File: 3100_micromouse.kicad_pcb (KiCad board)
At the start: 2 copper layers, 76 x 76 mm, 31 parts, among them J1 MOTOR1, J10 Extra +3.3V, J11 Extra +5V, J12 Extra +5V, J2 MOTOR2, J3 Extra GPIO A, J4 Extra GPIO B, J5 2 Pin PWR, J6 Aux SPI Bus, J7 Aux I2C Bus, J8 Extra Analog Pins, J9 UART Interface, U1 AMS1117-5.0

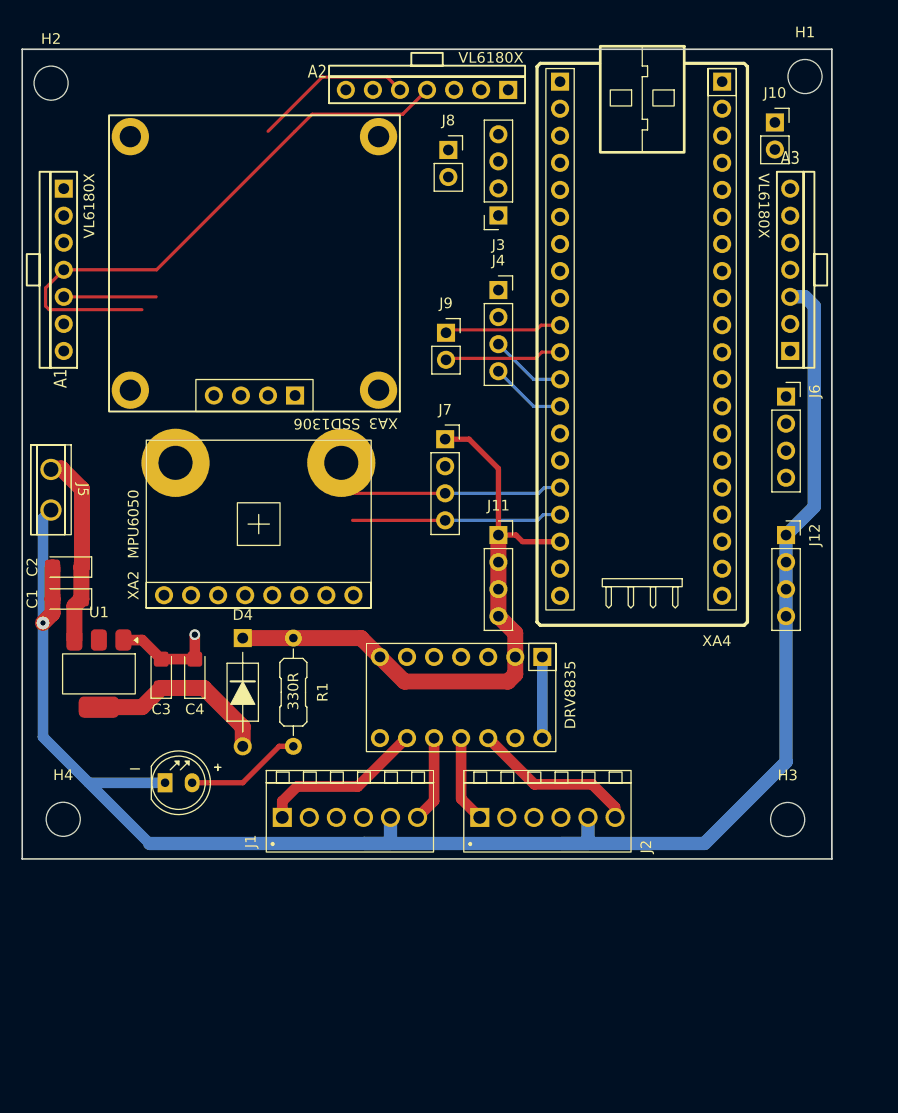
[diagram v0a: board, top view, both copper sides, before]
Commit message: Changed TOF Trigger pins to B12-14 - also removed 3V3 access as board space are running out
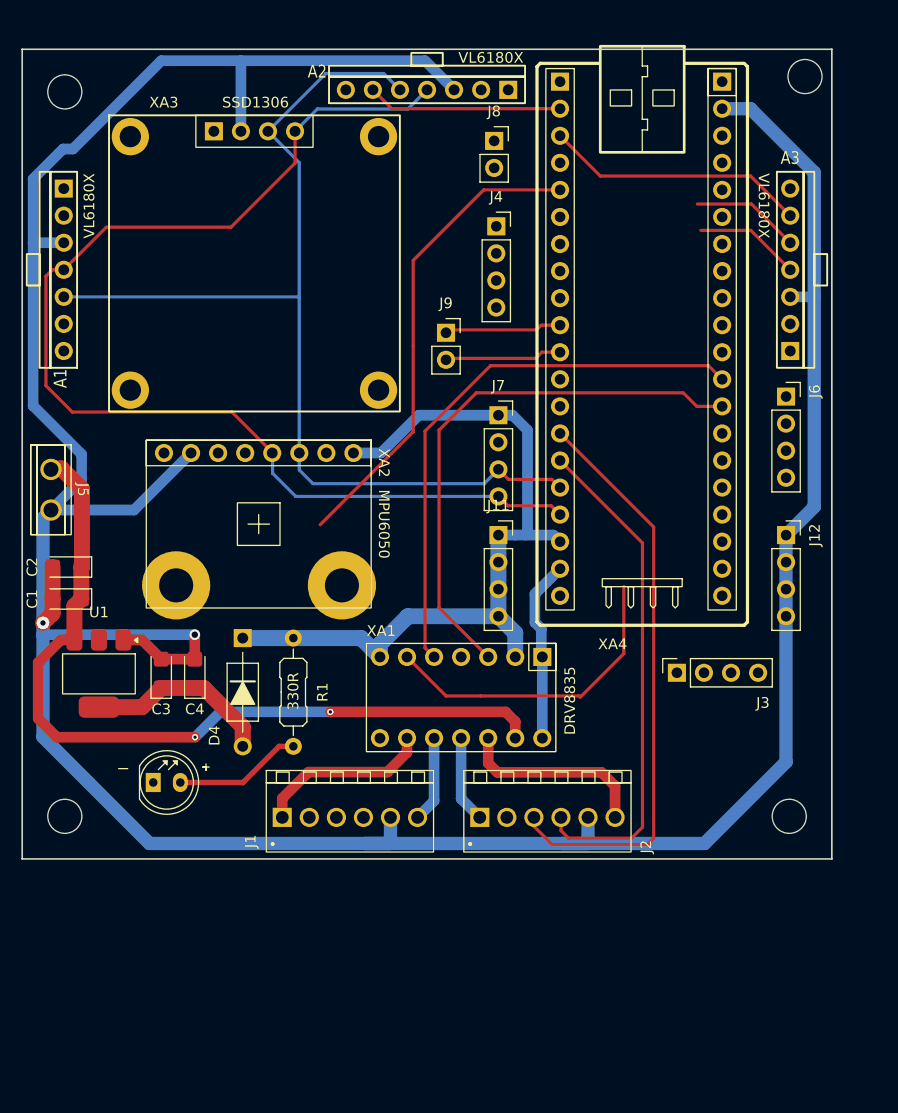
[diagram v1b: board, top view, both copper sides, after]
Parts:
- removed J10: Extra +3.3V, Connector_PinSocket_2.54mm:PinSocket_1x02_P2.54mm_Vertical
- moved J3 46.1 mm to (190.8, 102.9), turned to 90 degrees
- moved J4 5.98 mm to (173.8, 61.0)
- moved J7 5.48 mm to (174.0, 78.8)
- moved J8 4.38 mm to (173.6, 53.0)
- moved H2 1.53 mm to (133.3, 48.4)
- moved D1 1.11 mm to (141.6, 113.2)
- moved H3 0.34 mm to (201.3, 116.4)
- moved H4 0.32 mm to (133.3, 116.4)
- turned XA2 to -90 degrees
- turned XA3 to 0 degrees
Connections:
- J3 pad 1: /B12 -> /C12
- J3 pad 2: /B13 -> /C13
- J3 pad 3: /B14 -> /C14
- XA1 pad 13: VIN -> +9V
- XA4 pad 1: /B12 -> /TRIG1
- XA4 pad 2: /B13 -> /TRIG2
- XA4 pad 22: /TRIG1 -> /C12
- XA4 pad 23: /TRIG2 -> /C13
- XA4 pad 24: /TRIG3 -> /C14
- XA4 pad 3: /B14 -> /TRIG3
- XA4 pad 38: /+3V3 -> /STM32F411 Breakout Pin/+3V3
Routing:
- net GNDREF: track 185.1 -> 329.4 mm
- net /SCL: track 43.4 -> 106.9 mm
- net +9V: track 18.2 -> 76.2 mm, vias 0 -> 2
- net /ENC2A: track 0.00 -> 54.7 mm
- net /PWM1: track 0.00 -> 52.5 mm
- net /PWM2: track 0.00 -> 51.8 mm
- net /ENC2B: track 0.00 -> 47.2 mm
- net /SDA: track 74.1 -> 119.4 mm
- net /ENC1A: track 0.00 -> 44.9 mm
- net /DIR1: track 0.00 -> 29.9 mm
- net /TRIG3: track 0.00 -> 24.7 mm
- net /TRIG2: track 0.00 -> 18.3 mm
- net +5V: track 59.8 -> 74.3 mm
- net /B5: track 7.15 -> 0.00 mm
- net /B4: track 7.15 -> 0.00 mm
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
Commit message: Finialized and Finished PCB routing
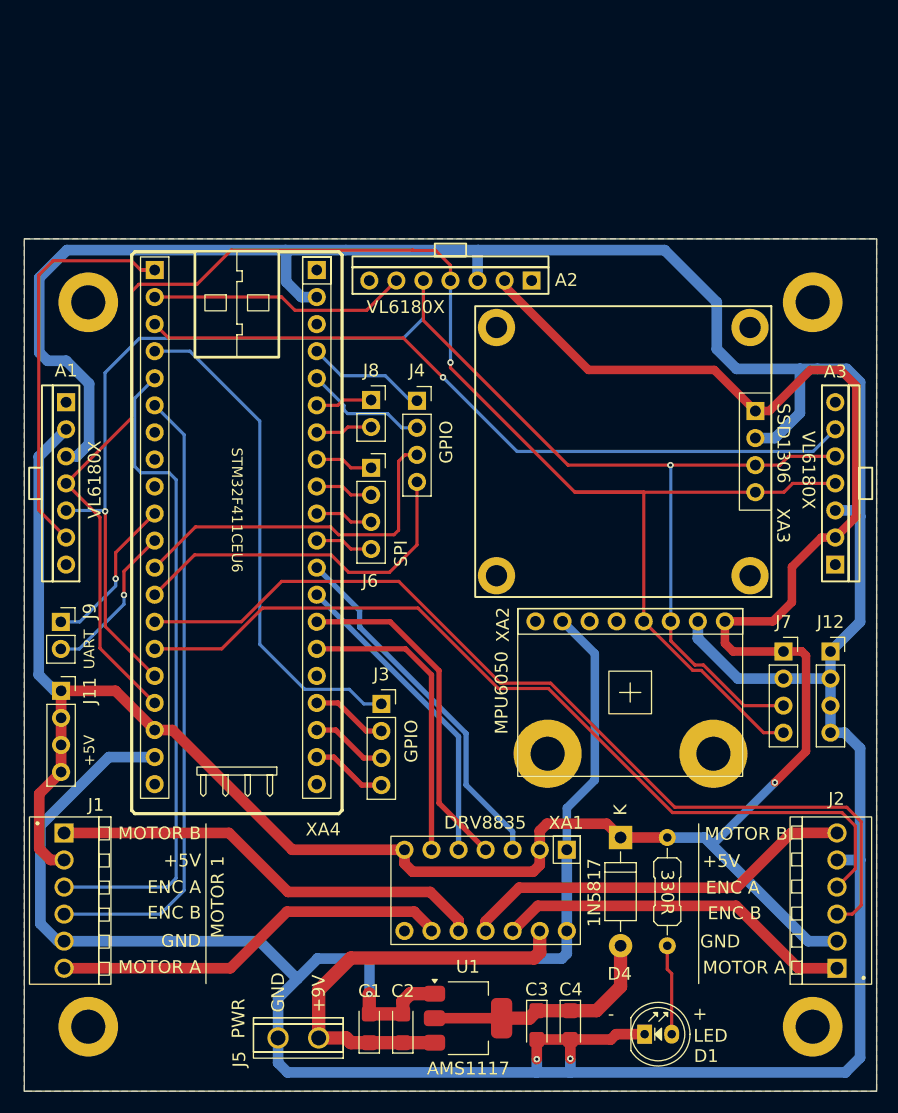
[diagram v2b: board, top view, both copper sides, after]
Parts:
- H1, H2, H3, H4: footprint MountingHole:MountingHole_3.2mm_M3 -> MountingHole:MountingHole_3.2mm_M3_DIN965_Pad
- moved J5 56.4 mm to (155.2, 137.2), turned to 180 degrees
- moved C2 53.6 mm to (165.0, 136.3), turned to 90 degrees
- moved D1 51.8 mm to (187.7, 136.8)
- moved C1 49.3 mm to (161.9, 136.3), turned to 90 degrees
- moved C3 48.3 mm to (177.6, 136.0), turned to -90 degrees
- moved C4 48.3 mm to (180.8, 136.0), turned to -90 degrees
- moved U1 47.4 mm to (171.2, 135.3), turned to 0 degrees
- moved J9 45.2 mm to (132.9, 98.2)
- moved J11 43.6 mm to (132.9, 104.6)
- moved XA4 42.0 mm to (149.4, 87.7)
- moved D4 40.1 mm to (185.5, 118.4)
- moved R1 39.8 mm to (189.8, 118.4)
- moved J6 39.5 mm to (162.1, 83.7)
- moved XA3 38.9 mm to (185.7, 82.2), turned to -90 degrees
- moved XA2 38.3 mm to (186.4, 104.8)
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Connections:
- net /A10 renamed /STM32F411 Breakout Pin/A10
- J1 pad 1: /MOTOR1A -> /MOTOR1B
- J1 pad 6: /MOTOR1B -> /MOTOR1A
- J2 pad 1: /MOTOR2A -> /MOTOR2B
- J2 pad 6: /MOTOR2B -> /MOTOR2A
- J3 pad 1: /C12 -> /B15
- J3 pad 2: /C13 -> /C14
- J3 pad 3: /C14 -> /C13
- J3 pad 4: /B15 -> /C12
- XA4 pad 28: /PWM2 -> /PWM1
- XA4 pad 29: /PWM1 -> /PWM2
- XA4 pad 40: /STM32F411 Breakout Pin/+5V_AUX -> +5V
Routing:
- net +5V: track 74.3 -> 237.2 mm, vias 0 -> 1
- net GNDREF: track 329.4 -> 414.8 mm, vias 2 -> 3
- net /ENC1B: track 0.00 -> 58.9 mm
- net /B15: track 0.00 -> 47.3 mm
- net /TRIG3: track 24.7 -> 69.7 mm, vias 0 -> 1
- net /SDA: track 119.4 -> 163.7 mm, vias 0 -> 1
- net /SCL: track 106.9 -> 147.6 mm, vias 0 -> 2
- net /TRIG1: track 0.00 -> 38.8 mm
- net +9V: track 76.2 -> 39.8 mm, vias 2 -> 0
- net /ENC2B: track 47.2 -> 82.3 mm
- net /B5: track 0.00 -> 33.8 mm
- net /B4: track 0.00 -> 33.4 mm
- net /MOTOR1B: track 8.08 -> 41.4 mm
- net /ENC2A: track 54.7 -> 87.7 mm
- net /DIR2: track 0.00 -> 32.0 mm
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- added copper zone on B.Cu, net GNDREF
- added copper zone on F.Cu, net GNDREF
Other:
- board size 76 x 76 mm -> 80 x 80 mm
- board text added: "+5V"
- board text added: "+9V"
- board text added: "1N5817"
- board text added: "AMS1117"
- board text added: "DRV8835"
- board text added: "ENC A"
- board text added: "ENC B"
- board text added: "GND"
- board text added: "GPIO"
- board text added: "LED"
- board text added: "MOTOR 1"
- board text added: "MOTOR A"
- board text added: "MOTOR B"
- board text added: "MPU6050"
- board text added: "PWR"
- board text added: "SPI"
- board text added: "SSD1306"
- board text added: "STM32F411CEU6"
- board text added: "UART"
- board text added: "VL6180X"
